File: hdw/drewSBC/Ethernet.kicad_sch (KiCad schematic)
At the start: 23 parts

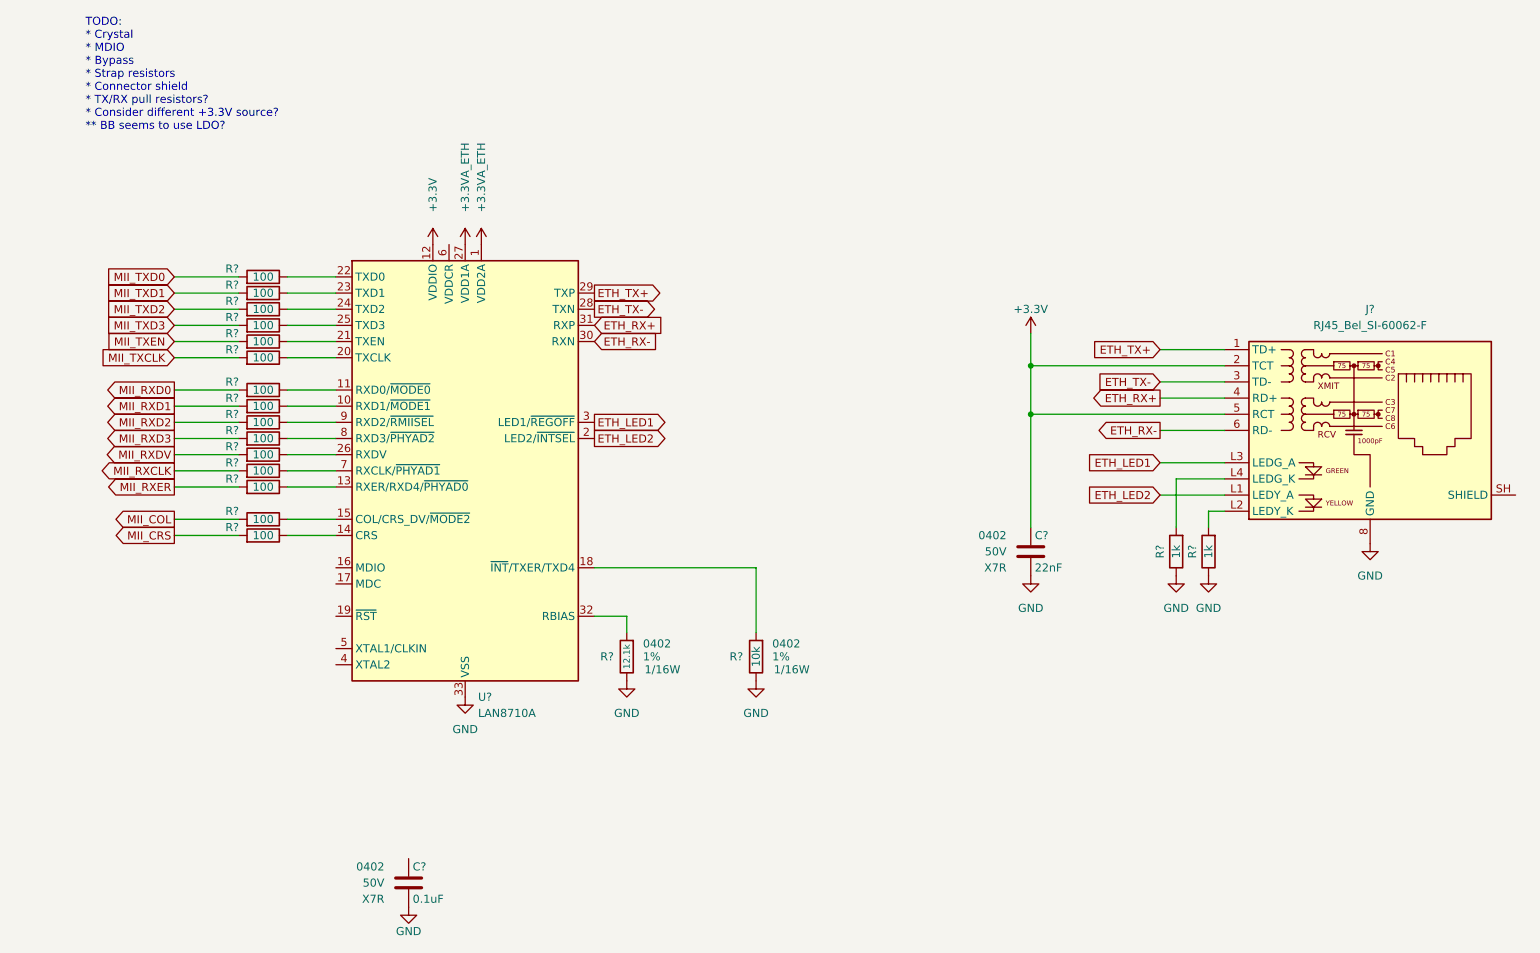
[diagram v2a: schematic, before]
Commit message: ripped up ETH phy
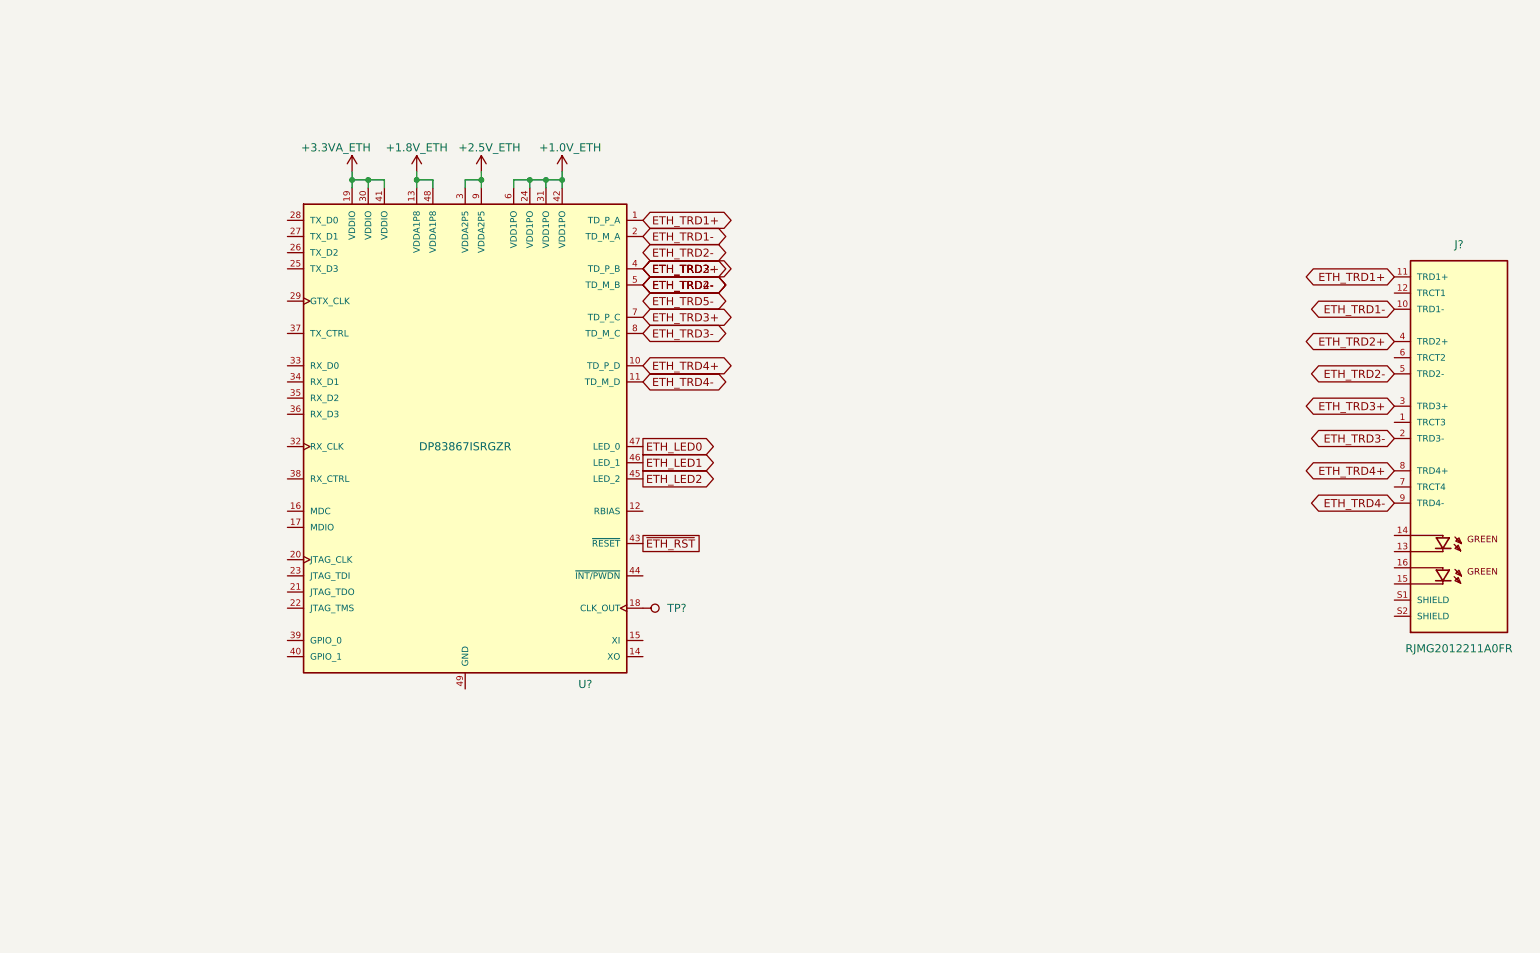
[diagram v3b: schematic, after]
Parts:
- removed C?: 0.1uF, Capacitors_SMD:C_0402, symbol Custom_Library:C_Custom
- removed C?: 22nF, Capacitors_SMD:C_0402, symbol Custom_Library:C_Custom
- removed J?: RJ45_Bel_SI-60062-F, Connector_RJ:RJ45_Bel_SI-60062-F, symbol Connector:RJ45_Bel_SI-60062-F
- removed R? (x15): 100, Resistors_SMD:R_0402, symbol Custom_Library:R_Custom
- removed R? (x2): 1k, Resistors_SMD:R_0402, symbol Custom_Library:R_Custom
- removed R?: 10k, Resistors_SMD:R_0402, symbol Custom_Library:R_Custom
- removed R?: 12.1k, Resistors_SMD:R_0402, symbol Custom_Library:R_Custom
- removed U?: LAN8710A, Package_DFN_QFN:QFN-32-1EP_5x5mm_P0.5mm_EP3.3x3.3mm_ThermalVias, symbol Interface_Ethernet:LAN8710A
- added J?: RJMG2012211A0FR, AMPHENOL_RJMG2012211A0FR, symbol Custom Library:RJMG2012211A0FR
- added TP?: TP, TestPoint:TestPoint_Keystone_5005-5009_Compact, symbol Custom Library:TP
- added U?: DP83867ISRGZR, Package_DFN_QFN:VQFN-48-1EP_7x7mm_P0.5mm_EP4.1x4.1mm, symbol Custom Library:DP83867ISRGZR
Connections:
- net +3.3VA_ETH: now also U?.19 (VDDIO), U?.30 (VDDIO), U?.41 (VDDIO)
- net ETH_LED1: now also U?.46 (LED_1)
- net ETH_LED2: now also U?.45 (LED_2)
- new net: TP?.1 (TP), U?.18 (CLK_OUT)
- new net +1.0V_ETH: U?.24 (VDD1PO), U?.31 (VDD1PO), U?.42 (VDD1PO), U?.6 (VDD1PO)
- new net +1.8V_ETH: U?.13 (VDDA1P8), U?.48 (VDDA1P8)
- new net +2.5V_ETH: U?.3 (VDDA2P5), U?.9 (VDDA2P5)
- new net ETH_LED0: U?.47 (LED_0)
- new net ETH_TRD1+: J?.11 (TRD1+), U?.1 (TD_P_A)
- new net ETH_TRD1-: J?.10 (TRD1-), U?.2 (TD_M_A)
- new net ETH_TRD2+: J?.2 (TRD3-), J?.4 (TRD2+), U?.4 (TD_P_B), U?.8 (TD_M_C)
- new net ETH_TRD2-: J?.5 (TRD2-), J?.9 (TRD4-), U?.11 (TD_M_D), U?.5 (TD_M_B)
- new net ETH_TRD3+: J?.3 (TRD3+), U?.7 (TD_P_C)
- new net ETH_TRD4+: J?.8 (TRD4+), U?.10 (TD_P_D)
- new net ~{ETH_RST}: U?.43 (~{RESET})
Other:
- note removed: "TODO: * Crystal * MDIO * Bypass * Strap resistors * Connector shield * TX/RX pull resistors? * Consider different +3.3V source? ** BB seems to use LDO?"

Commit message: more GB Ethernet work
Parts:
- added C? (x2): 0.1uF, Capacitors_SMD:C_0402, symbol Custom_Library:C_Custom
- added R? (x14): 10, Resistors_SMD:R_0402, symbol Custom_Library:R_Custom
- added R? (x2): 10k, Resistors_SMD:R_0402, symbol Custom_Library:R_Custom
- added R? (x3): 1k, Resistors_SMD:R_0402, symbol Custom_Library:R_Custom
- added R?: 2.49k, Resistors_SMD:R_0402, symbol Custom_Library:R_Custom
- added R?: 11k, Resistors_SMD:R_0402, symbol Custom_Library:R_Custom
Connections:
- net +3.3VA_ETH: now also R?.2
- net ETH_LED0: now also R?.1
- net ETH_LED2: now also R?.1
- net ETH_TRD2+: no longer J?.2 (TRD3-), U?.8 (TD_M_C)
- net ETH_TRD2-: no longer J?.9 (TRD4-), U?.11 (TD_M_D)
- net at U?.12 (RBIAS): now also R?.1
- net ETH_XO: now reaches U?.14 (XO)
- net ETH_XI: now reaches U?.15 (XI)
- net at U?.16 (MDC): now also R?.1, R?.2
- net at U?.17 (MDIO): now also R?.1, R?.2
- net at U?.25 (TX_D3): now also R?.2
- net at U?.26 (TX_D2): now also R?.2
- net at U?.27 (TX_D1): now also R?.2
- net at U?.28 (TX_D0): now also R?.2
- net at U?.29 (GTX_CLK): now also R?.2
- net at U?.32 (RX_CLK): now also R?.2
- net at U?.33 (RX_D0): now also R?.2
- net at U?.34 (RX_D1): now also R?.2
- net at U?.35 (RX_D2): now also R?.2
- net at U?.36 (RX_D3): now also R?.2
- net at U?.37 (TX_CTRL): now also R?.2
- net at U?.38 (RX_CTRL): now also R?.2
- net ETH_GPIO0: now reaches U?.39 (GPIO_0)
- net ETH_GPIO1: now reaches U?.40 (GPIO_1)
- net ~{ETH_INT}: now reaches U?.44 (~{INT/PWDN})
- net ~{ETH_INT}: now also R?.1
- net GND: now reaches U?.49 (GND)
- net GND: now also J?.13, J?.15, C?.2, C?.2, R?.2
- net at J?.1 (TRCT3): now also J?.12 (TRCT1), J?.6 (TRCT2), J?.7 (TRCT4), C?.1, C?.1, R?.2
- net at J?.14: now also R?.2
- net at J?.16: now also R?.2
- net +1.8V_ETH: no longer names the net of U?.13 (VDDA1P8)
- net +1.8V_ETH: no longer U?.48 (VDDA1P8)
- net +2.5V_ETH renamed +2.5VA_ETH
- net +2.5VA_ETH: now also R?.1
- new net +3.3V: R?.2, R?.2
- new net ETH_TRD3-: J?.2 (TRD3-), U?.8 (TD_M_C)
- new net ETH_TRD4-: J?.9 (TRD4-), U?.11 (TD_M_D)
- new net MDIO_MDC: R?.1
- new net MDIO_MDIO: R?.1
- new net RGMII0_RXCLK: R?.1
- new net RGMII0_RXCTL: R?.1
- new net RGMII0_RXD0: R?.1
- new net RGMII0_RXD1: R?.1
- new net RGMII0_RXD2: R?.1
- new net RGMII0_RXD3: R?.1
- new net RGMII0_TXCLK: R?.1
- new net RGMII0_TXCTL: R?.1
- new net RGMII0_TXD0: R?.1
- new net RGMII0_TXD1: R?.1
- new net RGMII0_TXD2: R?.1
- new net RGMII0_TXD3: R?.1
- no-connect marks 0 -> 8
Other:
- moved on the sheet: J?, TP?, U?
